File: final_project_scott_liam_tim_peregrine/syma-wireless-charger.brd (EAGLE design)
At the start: 90.5 x 64.5 mm, 46 parts, among them U1 SAMD21E

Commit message: fixed errors, added aesthetic silkscreen
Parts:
- moved U$3 1.00 mm to (9.02, 75.5)
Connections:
- removed net N$8: C1.2, R6.1, U$1.IMON
- net IMON: now also C1.2, R6.1, U$1.IMON
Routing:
- net GND: track 143.0 -> 120.4 mm
- net N$8: track 10.3 -> 0.00 mm
- net IMON: track 0.00 -> 10.3 mm
- net +5V: track 166.9 -> 165.6 mm
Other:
- board size 90.5 x 64.5 mm -> 90.5 x 53.5 mm
- board text added: "+"
- board text added: "Frustration of Electronics Wireless Charger Transmitter Board"
- board text added: "Peregrine Badger Tim McNamara Liam Mulshine Scott Sun"
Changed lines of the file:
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@@
 <?xml version="1.0" encoding="utf-8"?>
 <!DOCTYPE eagle SYSTEM "eagle.dtd">
-<eagle version="7.4.0">
+<eagle version="7.5.0">
 <drawing>
 <settings>
@@
 <layer number="43" name="vRestrict" color="2" fill="10" visible="yes" active="yes"/>
 <layer number="44" name="Drills" color="7" fill="1" visible="no" active="yes"/>
-<layer number="45" name="Holes" color="7" fill="1" visible="no" active="yes"/>
+<layer number="45" name="Holes" color="7" fill="1" visible="yes" active="yes"/>
 <layer number="46" name="Milling" color="3" fill="1" visible="no" active="yes"/>
 <layer number="47" name="Measures" color="7" fill="1" visible="no" active="yes"/>
@@
 <board>
 <plain>
-<wire x1="0" y1="15.5" x2="90.5" y2="15.5" width="0" layer="20"/>
-<wire x1="90.5" y1="15.5" x2="90.5" y2="80" width="0" layer="20"/>
+<wire x1="0" y1="26.5" x2="90.5" y2="26.5" width="0" layer="20"/>
+<wire x1="90.5" y1="26.5" x2="90.5" y2="80" width="0" layer="20"/>
 <wire x1="90.5" y1="80" x2="0" y2="80" width="0" layer="20"/>
-<wire x1="0" y1="80" x2="0" y2="15.5" width="0" layer="20"/>
+<wire x1="0" y1="80" x2="0" y2="26.5" width="0" layer="20"/>
+<hole x="88" y="77.5" drill="3.2"/>
+<hole x="88" y="29" drill="3.2"/>
+<hole x="2.5" y="29" drill="3.2"/>
+<hole x="2.5" y="77.5" drill="3.2"/>
+<text x="72" y="31.5" size="1.27" layer="21">Peregrine Badger
+Tim McNamara
+Liam Mulshine
+Scott Sun
+</text>
+<text x="33" y="58" size="1.016" layer="21">Frustration of Electronics
+Wireless Charger
+Transmitter Board</text>
+<text x="5" y="75" size="1.27" layer="21">+</text>
 </plain>
 <attributes>
@@
 <attribute name="VALUE" x="83.2" y="54.62" size="1.27" layer="21" rot="R270"/>
 </element>
-<element name="U$3" library="foe-scale" package="1X02" value="1X02" x="8.02" y="75.51"/>
+<element name="U$3" library="foe-scale" package="1X02" value="1X02" x="9.02" y="75.51"/>
 <element name="U$4" library="foe-scale" package="RGBLED" value="RGBLED" x="45.17" y="43.08" smashed="yes" rot="R180">
 <attribute name="VALUE" x="47.59" y="48.215" size="1.27" layer="21" rot="R180"/>
@@
 <wire x1="6.43" y1="69.07" x2="6" y2="69.5" width="1.016" layer="1"/>
 <via x="6" y="69.5" extent="1-16" drill="0.6"/>
-<wire x1="6" y1="69.5" x2="3" y2="72.5" width="1.016" layer="16"/>
-<via x="3" y="72.5" extent="1-16" drill="0.6"/>
-<wire x1="3" y1="72.5" x2="3" y2="75" width="1.016" layer="1"/>
-<wire x1="3" y1="75" x2="3.5" y2="75.5" width="1.016" layer="1"/>
-<wire x1="3.5" y1="75.5" x2="6.74" y2="75.5" width="1.016" layer="1"/>
-<wire x1="6.74" y1="75.5" x2="6.75" y2="75.51" width="1.016" layer="1"/>
+<wire x1="6" y1="69.5" x2="3.5" y2="72.5" width="1.016" layer="16"/>
+<via x="3.5" y="72.5" extent="1-16" drill="0.6"/>
+<wire x1="3.5" y1="72.5" x2="5" y2="75.5" width="1.016" layer="1"/>
+<wire x1="5" y1="75.5" x2="6.74" y2="75.5" width="1.016" layer="1"/>
+<wire x1="6.74" y1="75.5" x2="7.75" y2="75.51" width="1.016" layer="1"/>
 <wire x1="6.43" y1="69.07" x2="6.43" y2="67.5" width="1.016" layer="1"/>
 <wire x1="6.43" y1="67.5" x2="6.43" y2="66.57" width="1.016" layer="1"/>
@@
 <wire x1="66.04" y1="75.12" x2="66.18" y2="74.98" width="0.8128" layer="1"/>
 <wire x1="66.18" y1="74.98" x2="14.52" y2="74.98" width="1.016" layer="1"/>
-<wire x1="14.52" y1="74.98" x2="11.5" y2="78" width="1.016" layer="1"/>
-<wire x1="11.5" y1="78" x2="7.5" y2="78" width="1.016" layer="1"/>
-<wire x1="7.5" y1="78" x2="7" y2="77.5" width="1.016" layer="1"/>
-<wire x1="7" y1="77.5" x2="7" y2="75.76" width="1.016" layer="1"/>
-<wire x1="7" y1="75.76" x2="6.75" y2="75.51" width="1.016" layer="1"/>
+<wire x1="14.52" y1="74.98" x2="13" y2="78" width="1.016" layer="1"/>
+<wire x1="13" y1="78" x2="9" y2="78" width="1.016" layer="1"/>
+<wire x1="9" y1="78" x2="7.5" y2="75.76" width="1.016" layer="1"/>
+<wire x1="7.5" y1="75.76" x2="7.75" y2="75.51" width="1.016" layer="1"/>
 <wire x1="66.18" y1="74.98" x2="51.98" y2="74.98" width="0.8128" layer="1"/>
 <wire x1="51.98" y1="74.98" x2="50.5" y2="73.5" width="0.8128" layer="1"/>
@@
 <vertex x="0" y="80"/>
 <vertex x="90.5" y="80"/>
-<vertex x="90.5" y="15.5"/>
-<vertex x="0" y="15.5"/>
+<vertex x="90.5" y="28"/>
+<vertex x="0" y="28"/>
 </polygon>
 <wire x1="23.172615625" y1="47.974296875" x2="23.172615625" y2="44.672615625" width="0.4064" layer="1"/>
@@
 <wire x1="1.945" y1="35.555" x2="2.5" y2="35" width="0.4064" layer="1"/>
 <via x="2.5" y="35" extent="1-16" drill="0.6"/>
-<wire x1="2.5" y1="35" x2="24.5" y2="23.5" width="0.4064" layer="16"/>
-<wire x1="24.5" y1="23.5" x2="25" y2="24" width="0.4064" layer="16"/>
+<wire x1="2.5" y1="35" x2="5" y2="33.5" width="0.4064" layer="16"/>
 <wire x1="31.5" y1="71.84" x2="31.55" y2="71.89" width="0.4064" layer="1"/>
 <wire x1="17.57" y1="57.48" x2="17.57" y2="58.93" width="0.4064" layer="1"/>
@@
 <wire x1="53.25" y1="55.6" x2="53.48" y2="55.37" width="0.3048" layer="1"/>
 </signal>
-<signal name="N$8">
-<contactref element="R6" pad="1"/>
-<contactref element="U$1" pad="IMON"/>
-<contactref element="C1" pad="2"/>
-<wire x1="62.43" y1="71.98" x2="62.43" y2="69.27" width="0.3048" layer="1"/>
-<wire x1="62.43" y1="69.27" x2="62.38" y2="69.22" width="0.3048" layer="1"/>
-<wire x1="66.43" y1="63.61" x2="66.43" y2="65.57" width="0.3048" layer="1"/>
-<wire x1="66.43" y1="65.57" x2="66" y2="66" width="0.3048" layer="1"/>
-<wire x1="66" y1="66" x2="65.6" y2="66" width="0.3048" layer="1"/>
-<wire x1="65.6" y1="66" x2="62.38" y2="69.22" width="0.3048" layer="1"/>
-</signal>
 <signal name="N$9">
 <contactref element="U$1" pad="FB"/>
@@
 <signal name="IMON">
 <contactref element="U1" pad="5"/>
+<contactref element="R6" pad="1"/>
+<contactref element="U$1" pad="IMON"/>
+<contactref element="C1" pad="2"/>
+<wire x1="62.43" y1="71.98" x2="62.43" y2="69.27" width="0.3048" layer="1"/>
+<wire x1="62.43" y1="69.27" x2="62.38" y2="69.22" width="0.3048" layer="1"/>
+<wire x1="66.43" y1="63.61" x2="66.43" y2="65.57" width="0.3048" layer="1"/>
+<wire x1="66.43" y1="65.57" x2="66" y2="66" width="0.3048" layer="1"/>
+<wire x1="66" y1="66" x2="65.6" y2="66" width="0.3048" layer="1"/>
+<wire x1="65.6" y1="66" x2="62.38" y2="69.22" width="0.3048" layer="1"/>
+<wire x1="17.845015625" y1="42.646696875" x2="62.38" y2="69.22" width="0" layer="19" extent="1-1"/>
 </signal>
 <signal name="ALIGNED">
@@
 </board>
 </drawing>
+<compatibility>
+<note version="6.3" minversion="6.2.2" severity="warning">
+Since Version 6.2.2 text objects can contain more than one line,
+which will not be processed correctly with this version.
+</note>
+</compatibility>
 </eagle>

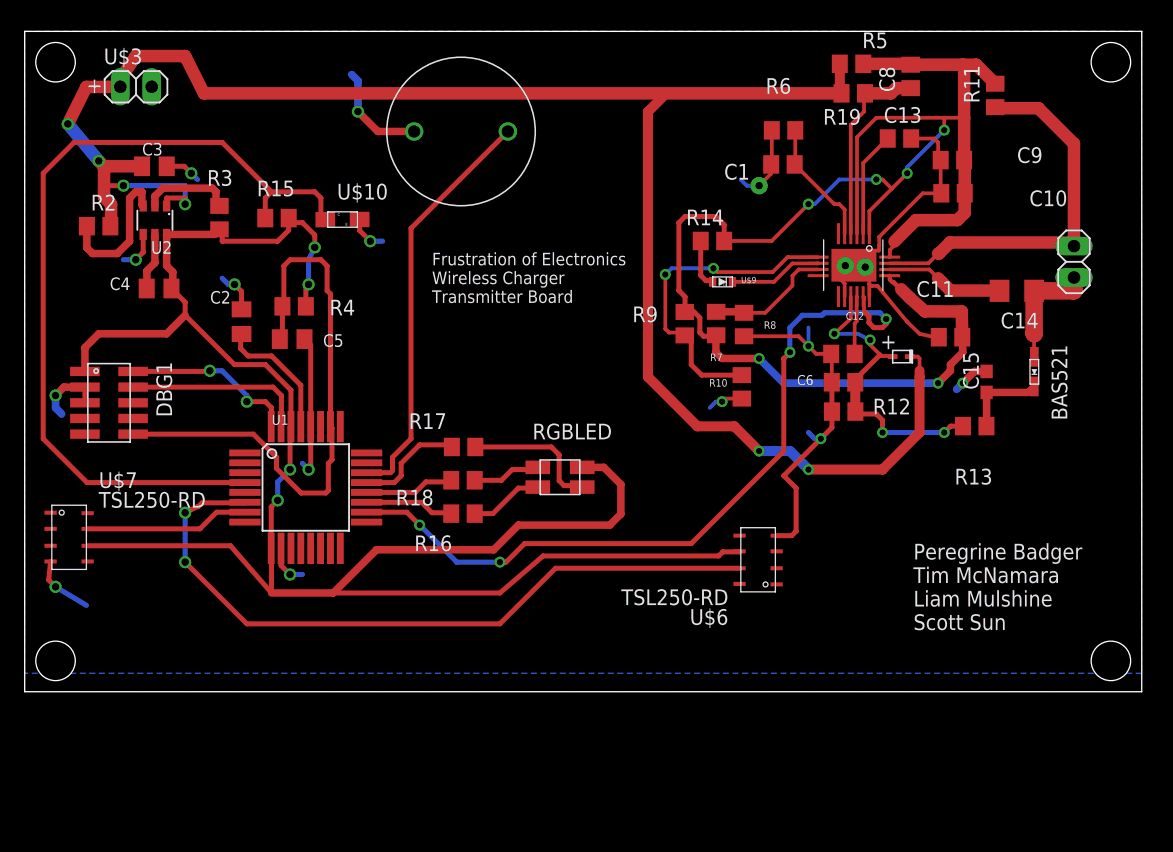
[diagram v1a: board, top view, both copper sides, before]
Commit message: Fixed ambient light sensor
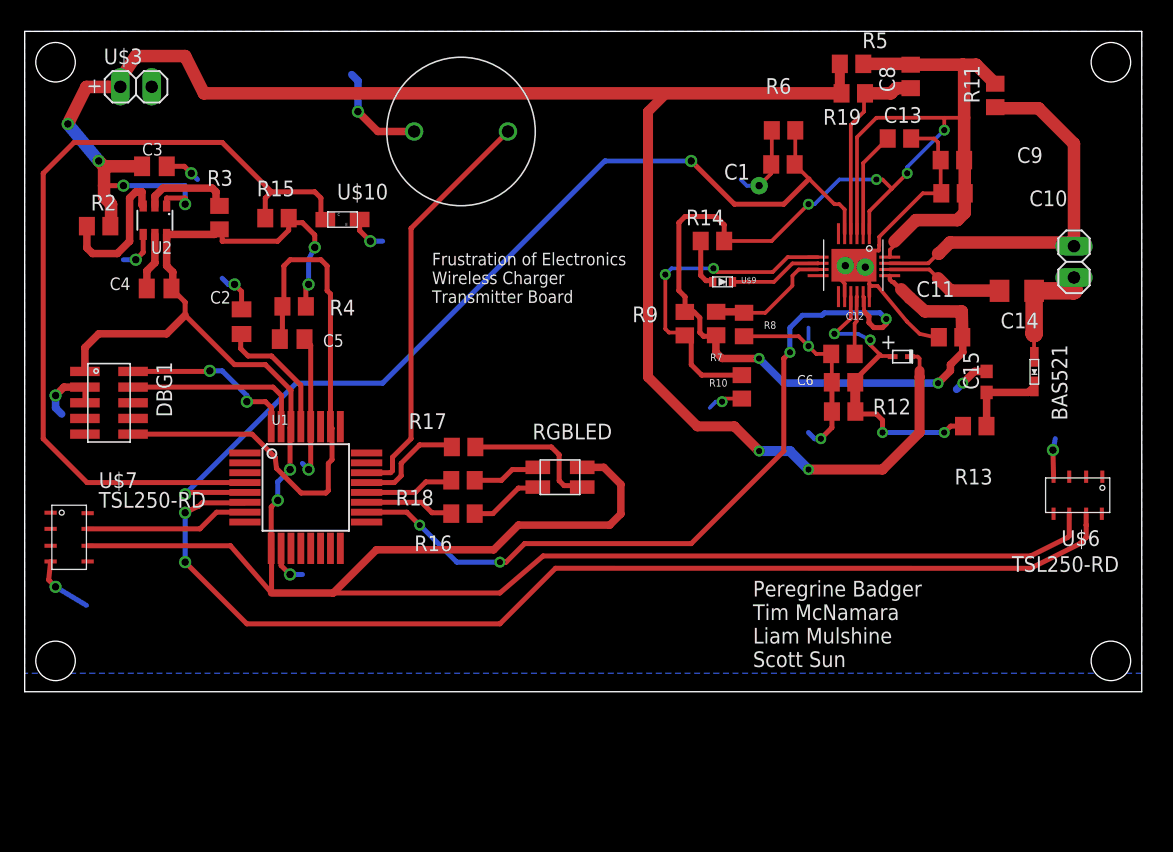
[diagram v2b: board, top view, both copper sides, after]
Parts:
- moved U$6 26.4 mm to (85.3, 42.4), turned to 270 degrees
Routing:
- net IMON: track 10.3 -> 79.3 mm, vias 0 -> 2
- net CARSENSE: track 58.0 -> 88.6 mm
- net VDD: track 160.4 -> 189.1 mm
- net GND: track 120.4 -> 112.6 mm, vias 16 -> 17
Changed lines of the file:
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@@
 <hole x="2.5" y="29" drill="3.2"/>
 <hole x="2.5" y="77.5" drill="3.2"/>
-<text x="72" y="31.5" size="1.27" layer="21">Peregrine Badger
+<text x="59" y="28.5" size="1.27" layer="21">Peregrine Badger
 Tim McNamara
 Liam Mulshine
@@
 </element>
 <element name="U$5" library="foe-scale" package="BUZZER" value="BUZZER" x="31.55" y="71.89" smashed="yes" rot="R270"/>
-<element name="U$6" library="foe-scale" package="TSL250-RD" value="TSL250-RD" x="59.42" y="37.19" smashed="yes" rot="R180">
-<attribute name="NAME" x="57.02" y="33.19" size="1.27" layer="21" rot="R180"/>
-<attribute name="VALUE" x="57.02" y="34.79" size="1.27" layer="21" rot="R180"/>
+<element name="U$6" library="foe-scale" package="TSL250-RD" value="TSL250-RD" x="85.31" y="42.42" smashed="yes" rot="R270">
+<attribute name="NAME" x="83.98" y="38.31" size="1.27" layer="21"/>
+<attribute name="VALUE" x="79.98" y="36.21" size="1.27" layer="21"/>
 </element>
 <element name="U$7" library="foe-scale" package="TSL250-RD" value="TSL250-RD" x="3.6" y="39.01" smashed="yes">
@@
 <via x="76" y="51.5" extent="1-16" drill="0.5"/>
 <wire x1="76" y1="51.5" x2="75.5" y2="51" width="0.6096" layer="16"/>
-<wire x1="60.92" y1="39.145" x2="62.145" y2="39.145" width="0.4064" layer="1"/>
-<wire x1="62.145" y1="39.145" x2="62.5" y2="39.5" width="0.4064" layer="1"/>
-<wire x1="62.5" y1="39.5" x2="62.5" y2="43" width="0.4064" layer="1"/>
-<wire x1="62.5" y1="43" x2="61.5" y2="44" width="0.4064" layer="1"/>
-<wire x1="61.5" y1="44" x2="64.5" y2="47" width="0.4064" layer="1"/>
+<wire x1="83.355" y1="43.92" x2="83.304415625" y2="46.07889375" width="0.4064" layer="1"/>
+<via x="83.304415625" y="46.07889375" extent="1-16" drill="0.6"/>
+<wire x1="83.304415625" y1="46.07889375" x2="83.5" y2="47" width="0.4064" layer="16"/>
 </signal>
 <signal name="N$3">
@@
 <wire x1="20" y1="34.5" x2="38.5" y2="34.5" width="0.4064" layer="1"/>
 <wire x1="38.5" y1="34.5" x2="42" y2="37.5" width="0.4064" layer="1"/>
-<wire x1="42" y1="37.5" x2="56.21871875" y2="37.5" width="0.4064" layer="1"/>
-<wire x1="56.21871875" y1="37.5" x2="56.550728125" y2="37.832009375" width="0.4064" layer="1"/>
 <contactref element="U$7" pad="VDD"/>
 <wire x1="5.1" y1="38.325" x2="16.675" y2="38.325" width="0.4064" layer="1"/>
 <wire x1="19.972615625" y1="38.119096875" x2="20" y2="38.119096875" width="0.4064" layer="1"/>
 <contactref element="U$6" pad="VDD"/>
-<wire x1="56.550728125" y1="37.832009375" x2="57.92" y2="37.832009375" width="0.4064" layer="1"/>
-<wire x1="57.92" y1="37.832009375" x2="57.92" y2="37.875" width="0.4064" layer="1"/>
+<wire x1="42" y1="37.5" x2="81.5" y2="37.5" width="0.4064" layer="1"/>
+<wire x1="81.5" y1="37.5" x2="84.5" y2="39" width="0.4064" layer="1"/>
+<wire x1="84.5" y1="39" x2="84.625" y2="39.125" width="0.4064" layer="1"/>
+<wire x1="84.625" y1="39.125" x2="84.625" y2="40.92" width="0.4064" layer="1"/>
 </signal>
 <signal name="N$2">
@@
 <wire x1="24.5" y1="61" x2="24.5" y2="59" width="0.4064" layer="1"/>
 <wire x1="24.5" y1="59" x2="24.772615625" y2="58.727384375" width="0.4064" layer="1"/>
-<wire x1="8.78" y1="47.37" x2="18.53" y2="47.37" width="0.4064" layer="1"/>
-<wire x1="18.53" y1="47.37" x2="20.4" y2="45.5" width="0.4064" layer="1"/>
-<wire x1="20.4" y1="45.5" x2="20.4" y2="44.6" width="0.4064" layer="1"/>
+<wire x1="8.78" y1="47.37" x2="18.422784375" y2="47.37" width="0.4064" layer="1"/>
+<wire x1="18.422784375" y1="47.37" x2="20.292784375" y2="45.5" width="0.4064" layer="1"/>
+<wire x1="20.292784375" y1="45.5" x2="20.4" y2="44.6" width="0.4064" layer="1"/>
 <wire x1="20.4" y1="44.6" x2="22.4" y2="42.6" width="0.4064" layer="1"/>
 <wire x1="22.4" y1="42.6" x2="24.4" y2="42.6" width="0.4064" layer="1"/>
@@
 <contactref element="U1" pad="6"/>
 <contactref element="U$6" pad="OUT"/>
-<wire x1="57.92" y1="36.505" x2="43.005" y2="36.505" width="0.4064" layer="1"/>
 <wire x1="43.005" y1="36.505" x2="38.5" y2="32" width="0.4064" layer="1"/>
 <wire x1="38.5" y1="32" x2="18" y2="32" width="0.4064" layer="1"/>
@@
 <wire x1="14.37279375" y1="41.804034375" x2="17.802353125" y2="41.804034375" width="0.4064" layer="1"/>
 <wire x1="17.802353125" y1="41.804034375" x2="17.845015625" y2="41.846696875" width="0.4064" layer="1"/>
+<wire x1="43.005" y1="36.505" x2="81.5" y2="36.5" width="0.4064" layer="1"/>
+<wire x1="81.5" y1="36.5" x2="85.5" y2="38.5" width="0.4064" layer="1"/>
+<wire x1="85.5" y1="38.5" x2="86" y2="39" width="0.4064" layer="1"/>
+<wire x1="86" y1="39" x2="86" y2="40" width="0.4064" layer="1"/>
+<wire x1="86" y1="40" x2="85.995" y2="40.005" width="0.4064" layer="1"/>
+<wire x1="85.995" y1="40.005" x2="85.995" y2="40.92" width="0.4064" layer="1"/>
 </signal>
 <signal name="IMON">
@@
 <wire x1="66.43" y1="65.57" x2="66" y2="66" width="0.3048" layer="1"/>
 <wire x1="66" y1="66" x2="65.6" y2="66" width="0.3048" layer="1"/>
-<wire x1="65.6" y1="66" x2="62.38" y2="69.22" width="0.3048" layer="1"/>
-<wire x1="17.845015625" y1="42.646696875" x2="62.38" y2="69.22" width="0" layer="19" extent="1-1"/>
+<wire x1="65.6" y1="66" x2="63.55" y2="68.05" width="0.3048" layer="1"/>
+<wire x1="63.55" y1="68.05" x2="62.38" y2="69.22" width="0.3048" layer="1"/>
+<wire x1="17.845015625" y1="42.646696875" x2="13" y2="42.646696875" width="0.4064" layer="1"/>
+<wire x1="13" y1="42.646696875" x2="13" y2="42.5" width="0.4064" layer="1"/>
+<via x="13" y="42.5" extent="1-16" drill="0.6"/>
+<wire x1="13" y1="42.5" x2="22" y2="51.5" width="0.4064" layer="16"/>
+<wire x1="22" y1="51.5" x2="29" y2="51.5" width="0.4064" layer="16"/>
+<wire x1="29" y1="51.5" x2="47" y2="69.5" width="0.4064" layer="16"/>
+<wire x1="47" y1="69.5" x2="54" y2="69.5" width="0.4064" layer="16"/>
+<via x="54" y="69.5" extent="1-16" drill="0.6"/>
+<wire x1="54" y1="69.5" x2="57.5" y2="66" width="0.4064" layer="1"/>
+<wire x1="57.5" y1="66" x2="61.5" y2="66" width="0.4064" layer="1"/>
+<wire x1="61.5" y1="66" x2="63.55" y2="68.05" width="0.4064" layer="1"/>
 </signal>
 <signal name="ALIGNED">

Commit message: minor error checking
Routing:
- net RST: track 46.8 -> 47.5 mm
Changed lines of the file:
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@@
 Scott Sun
 </text>
-<text x="33" y="58" size="1.016" layer="21">Frustration of Electronics
+<text x="30" y="56" size="1.27" layer="21">Frustration of Electronics
 Wireless Charger
 Transmitter Board</text>
@@
 <wire x1="8.78" y1="47.37" x2="18.422784375" y2="47.37" width="0.4064" layer="1"/>
 <wire x1="18.422784375" y1="47.37" x2="20.292784375" y2="45.5" width="0.4064" layer="1"/>
-<wire x1="20.292784375" y1="45.5" x2="20.4" y2="44.6" width="0.4064" layer="1"/>
-<wire x1="20.4" y1="44.6" x2="22.4" y2="42.6" width="0.4064" layer="1"/>
-<wire x1="22.4" y1="42.6" x2="24.4" y2="42.6" width="0.4064" layer="1"/>
+<wire x1="20.292784375" y1="45.5" x2="19.9" y2="44.6" width="0.4064" layer="1"/>
+<wire x1="19.9" y1="44.6" x2="21.4" y2="42.6" width="0.4064" layer="1"/>
+<wire x1="21.4" y1="42.6" x2="24.4" y2="42.6" width="0.4064" layer="1"/>
 <wire x1="24.4" y1="42.6" x2="24.6" y2="42.8" width="0.4064" layer="1"/>
 <wire x1="24.6" y1="42.8" x2="24.6" y2="45" width="0.4064" layer="1"/>
